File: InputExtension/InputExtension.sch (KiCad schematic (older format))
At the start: 10 parts, among them P1 CONN_01X04, P2 CONN_01X04, P3 CONN_01X08, P4 CONN_01X08, U1 PCF8574

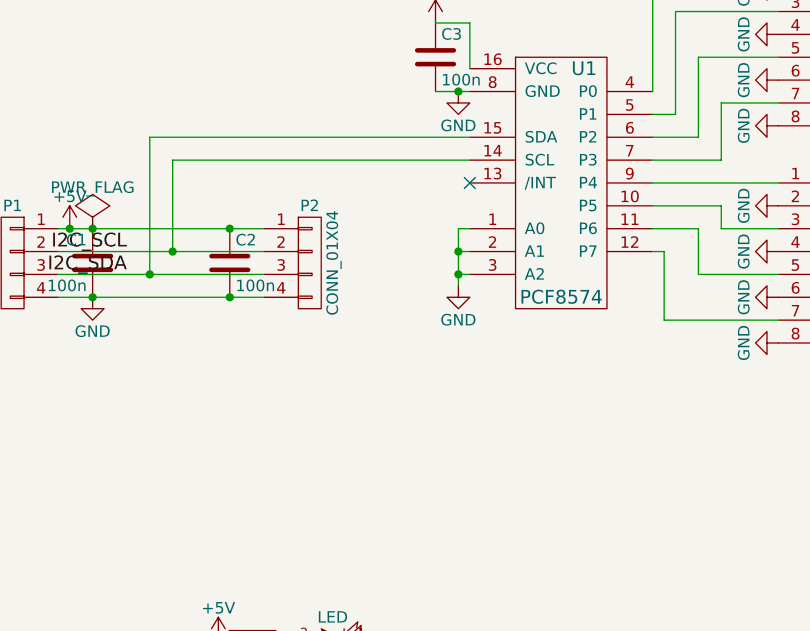
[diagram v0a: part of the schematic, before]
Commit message: Added the Input extension PCB layout
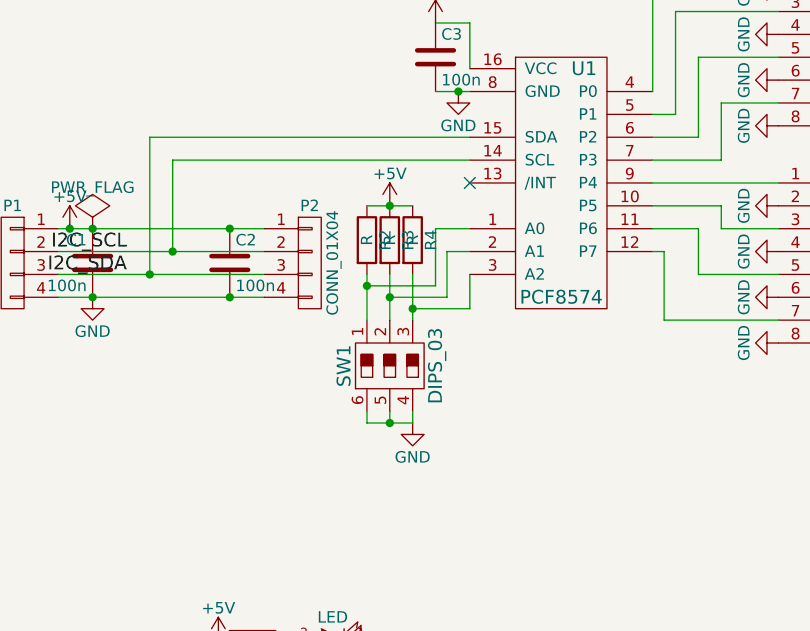
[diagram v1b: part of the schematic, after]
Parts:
- added R2, R3, R4: R, Resistors_SMD:R_0805_HandSoldering, symbol R
- added SW1: DIPS_03, dips-s:DIPS-DS03, symbol DIPS_03
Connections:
- net +5V: now also R2.1, R3.1, R4.1
- net GND: now also SW1.4, SW1.5, SW1.6; no longer U1.1 (A0), U1.2 (A1), U1.3 (A2)
- new net: R2.2, SW1.1, U1.1 (A0)
- new net: R3.2, SW1.2, U1.2 (A1)
- new net: R4.2, SW1.3, U1.3 (A2)
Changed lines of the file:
@@
 LIBS:contrib
 LIBS:valves
+LIBS:dips-s
 LIBS:InputExtension-cache
 EELAYER 25 0
@@
 L GND #PWR03
 U 1 1 568473E3
-P 4250 3300
-F 0 "#PWR03" H 4250 3050 50  0001 C CNN
-F 1 "GND" H 4250 3150 50  0000 C CNN
-F 2 "" H 4250 3300 50  0000 C CNN
-F 3 "" H 4250 3300 50  0000 C CNN
-	1    4250 3300
+P 4050 3900
+F 0 "#PWR03" H 4050 3650 50  0001 C CNN
+F 1 "GND" H 4050 3750 50  0000 C CNN
+F 2 "" H 4050 3900 50  0000 C CNN
+F 3 "" H 4050 3900 50  0000 C CNN
+	1    4050 3900
 	1    0    0    -1
 $EndComp
@@
 Wire Wire Line
 	4300 2150 4150 2150
-Wire Wire Line
-	4300 3050 4250 3050
-Wire Wire Line
-	4250 3050 4250 3300
-Wire Wire Line
-	4300 3250 4250 3250
-Connection ~ 4250 3250
-Wire Wire Line
-	4300 3150 4250 3150
-Connection ~ 4250 3150
 Connection ~ 2550 3050
 Wire Wire Line
@@
 	0    1    1    0
 $EndComp
+$Comp
+L DIPS_03 SW1
+U 1 1 568A622C
+P 3950 3650
+F 0 "SW1" V 3750 3650 60  0000 C CNN
+F 1 "DIPS_03" V 4150 3650 60  0000 C CNN
+F 2 "dips-s:DIPS-DS03" H 3950 3650 60  0001 C CNN
+F 3 "" H 3950 3650 60  0000 C CNN
+	1    3950 3650
+	1    0    0    1
+$EndComp
+Wire Wire Line
+	4050 3900 3850 3900
+Wire Wire Line
+	3850 3900 3850 3850
+Wire Wire Line
+	3950 3850 3950 3900
+Connection ~ 3950 3900
+Wire Wire Line
+	4050 3850 4050 3900
+$Comp
+L +5V #PWR017
+U 1 1 568A65EB
+P 3950 2950
+F 0 "#PWR017" H 3950 2800 50  0001 C CNN
+F 1 "+5V" H 3950 3090 50  0000 C CNN
+F 2 "" H 3950 2950 50  0000 C CNN
+F 3 "" H 3950 2950 50  0000 C CNN
+	1    3950 2950
+	1    0    0    -1
+$EndComp
+$Comp
+L R R2
+U 1 1 568A6615
+P 3850 3100
+F 0 "R2" V 3930 3100 50  0000 C CNN
+F 1 "R" V 3850 3100 50  0000 C CNN
+F 2 "Resistors_SMD:R_0805_HandSoldering" V 3780 3100 50  0001 C CNN
+F 3 "" H 3850 3100 50  0000 C CNN
+	1    3850 3100
+	1    0    0    -1
+$EndComp
+$Comp
+L R R3
+U 1 1 568A666E
+P 3950 3100
+F 0 "R3" V 4030 3100 50  0000 C CNN
+F 1 "R" V 3950 3100 50  0000 C CNN
+F 2 "Resistors_SMD:R_0805_HandSoldering" V 3880 3100 50  0001 C CNN
+F 3 "" H 3950 3100 50  0000 C CNN
+	1    3950 3100
+	1    0    0    -1
+$EndComp
+$Comp
+L R R4
+U 1 1 568A66A5
+P 4050 3100
+F 0 "R4" V 4130 3100 50  0000 C CNN
+F 1 "R" V 4050 3100 50  0000 C CNN
+F 2 "Resistors_SMD:R_0805_HandSoldering" V 3980 3100 50  0001 C CNN
+F 3 "" H 4050 3100 50  0000 C CNN
+	1    4050 3100
+	1    0    0    -1
+$EndComp
+Wire Wire Line
+	3850 2950 4050 2950
+Connection ~ 3950 2950
+Wire Wire Line
+	3850 3250 3850 3450
+Wire Wire Line
+	3950 3250 3950 3450
+Wire Wire Line
+	4050 3250 4050 3450
+Wire Wire Line
+	4300 3050 4150 3050
+Wire Wire Line
+	4150 3050 4150 3300
+Wire Wire Line
+	4150 3300 3850 3300
+Connection ~ 3850 3300
+Wire Wire Line
+	3950 3350 4200 3350
+Wire Wire Line
+	4200 3350 4200 3150
+Wire Wire Line
+	4200 3150 4300 3150
+Connection ~ 3950 3350
+Wire Wire Line
+	4300 3250 4300 3400
+Wire Wire Line
+	4300 3400 4050 3400
+Connection ~ 4050 3400
 $EndSCHEMATC

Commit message: Add new input extension pcb
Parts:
- removed C1, C2: 100n, Capacitors_ThroughHole:C_Disc_D12_P7.75, symbol C
- removed C3: 100n, Capacitors_SMD:C_0805_HandSoldering, symbol C
- removed D1: LED, LEDs:LED-0805, symbol LED
- removed P1, P2: CONN_01X04, Pin_Headers:Pin_Header_Straight_1x04, symbol CONN_01X04
- removed P3, P4: CONN_01X08, Pin_Headers:Pin_Header_Straight_1x08, symbol CONN_01X08
- removed R1: 220, Resistors_SMD:R_0805_HandSoldering, symbol R
- removed R2, R3, R4: R, Resistors_SMD:R_0805_HandSoldering, symbol R
- removed SW1: DIPS_03, dips-s:DIPS-DS03, symbol DIPS_03
- removed U1: PCF8574, Housings_SOIC:SOIC-16_7.5x10.3mm_Pitch1.27mm, symbol PCA9534
- added C1, C2, C3: 1u, Capacitor_SMD:C_0805_2012Metric, symbol Device:C
- added D1: LED, LED_SMD:LED_0805_2012Metric, symbol Device:LED
- added J1, J2: Conn_01x04, Connector_PinHeader_2.54mm:PinHeader_1x04_P2.54mm_Vertical, symbol Connector_Generic:Conn_01x04
- added J3, J4: Conn_01x08, Connector_PinHeader_2.54mm:PinHeader_1x08_P2.54mm_Vertical, symbol Connector_Generic:Conn_01x08
- added JP1, JP2, JP3: JP, Connector_PinHeader_2.54mm:PinHeader_1x03_P2.54mm_Vertical, symbol Jumper:Jumper_3_Bridged12
- added R1: 220R, Resistor_SMD:R_0805_2012Metric, symbol Device:R
- added U1: PCF8574, Package_SO:SOIC-16W_7.5x10.3mm_P1.27mm, symbol Interface_Expansion:PCF8574
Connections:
- net labels added: A0, A1, A2
- wire segments 49 -> 65
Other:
- note added: "I2C Address = 0b0010<A2><A1><A0><R/W>"
- note added: "Second I2C port for\n * Daisy chaining\n * Termination pullups"
